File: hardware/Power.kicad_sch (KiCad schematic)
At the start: 16 parts, among them J200 Conn_Receptacle_2P, Q200 AO3401A, U200 RT9080-33GJ5, U201 TPS610997DRV, X200 12401598E4#2A

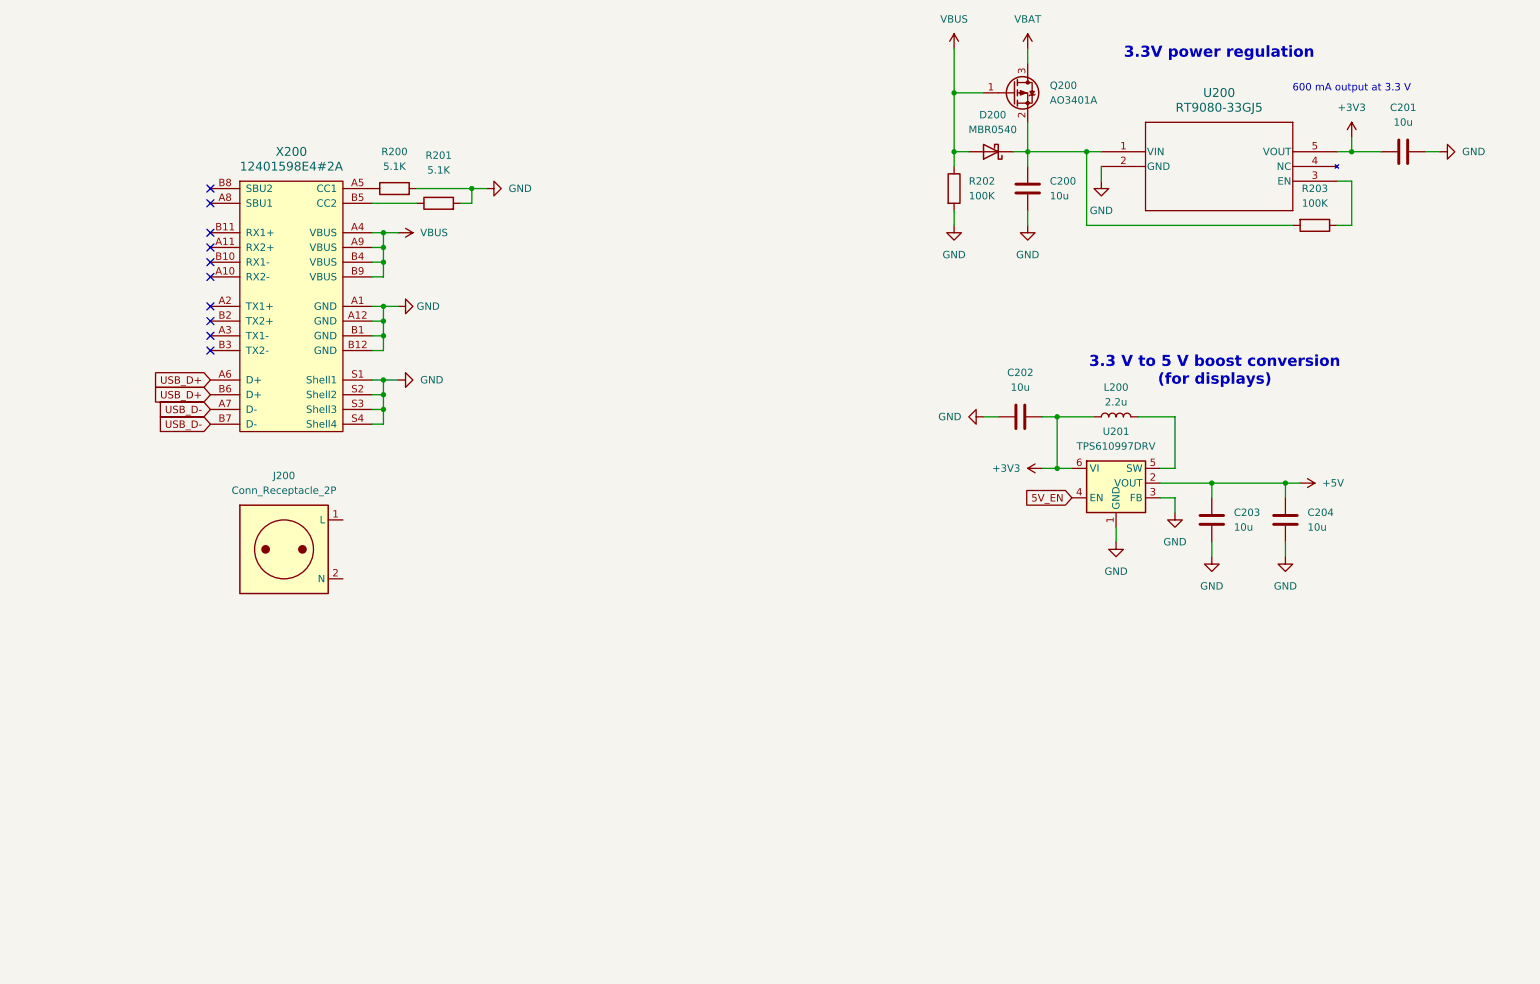
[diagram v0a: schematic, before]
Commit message: Modify 5V boost converter to use VBAT instead of 3V3 for input and add power switching circuit
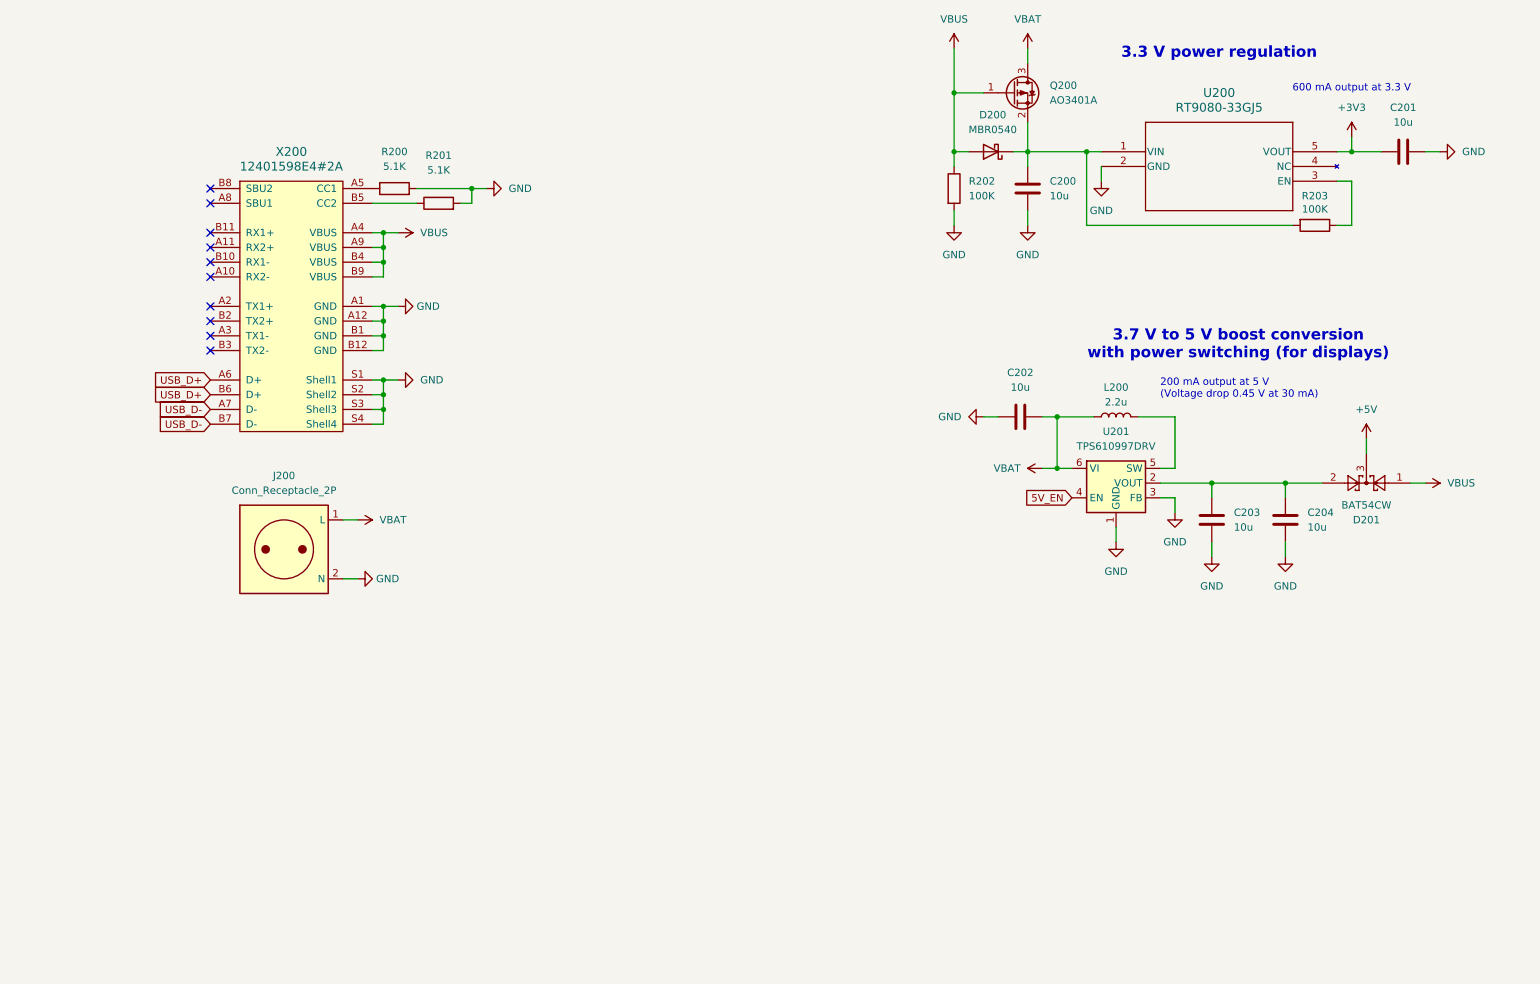
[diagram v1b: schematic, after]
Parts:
- added D201: BAT54CW, Package_TO_SOT_SMD:SOT-323_SC-70, symbol Diode:BAT54CW
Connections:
- net +3V3: no longer C202.2, L200.1, U201.6 (VI)
- net +5V: now also D201.3; no longer C203.1, C204.1, U201.2 (VOUT)
- net GND: now also J200.2 (N)
- net VBAT: now also C202.2, J200.1 (L), L200.1, U201.6 (VI)
- net VBUS: now also D201.1
- new net: C203.1, C204.1, D201.2, U201.2 (VOUT)
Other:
- note added: "200 mA output at 5 V (Voltage drop 0.45 V at 30 mA)"
- note added: "3.3 V power regulation"
- note added: "3.7 V to 5 V boost conversion with power switching (for displays)"
- note removed: "3.3 V to 5 V boost conversion (for displays)"
- note removed: "3.3V power regulation"

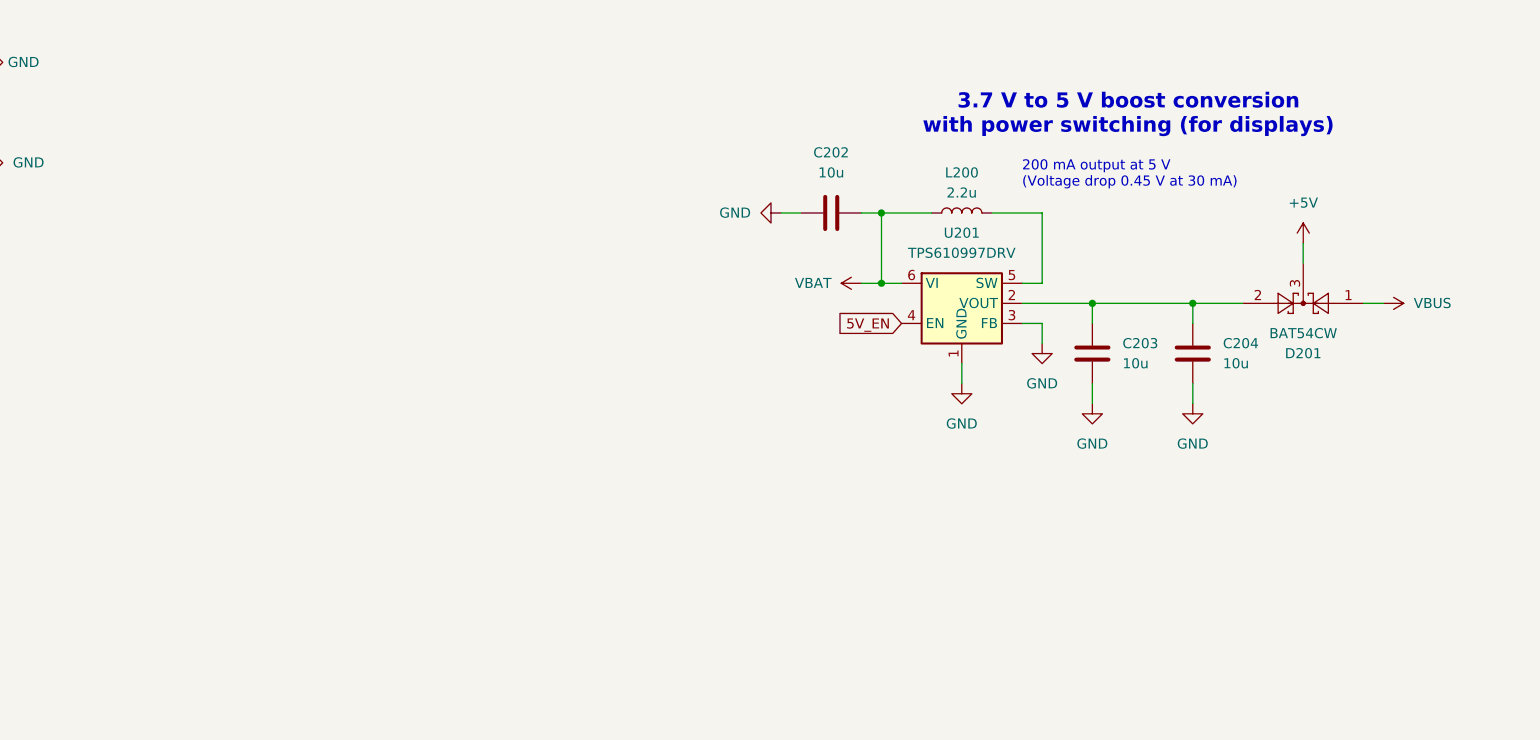
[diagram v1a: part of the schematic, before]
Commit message: Add voltage divider and replace boost converter
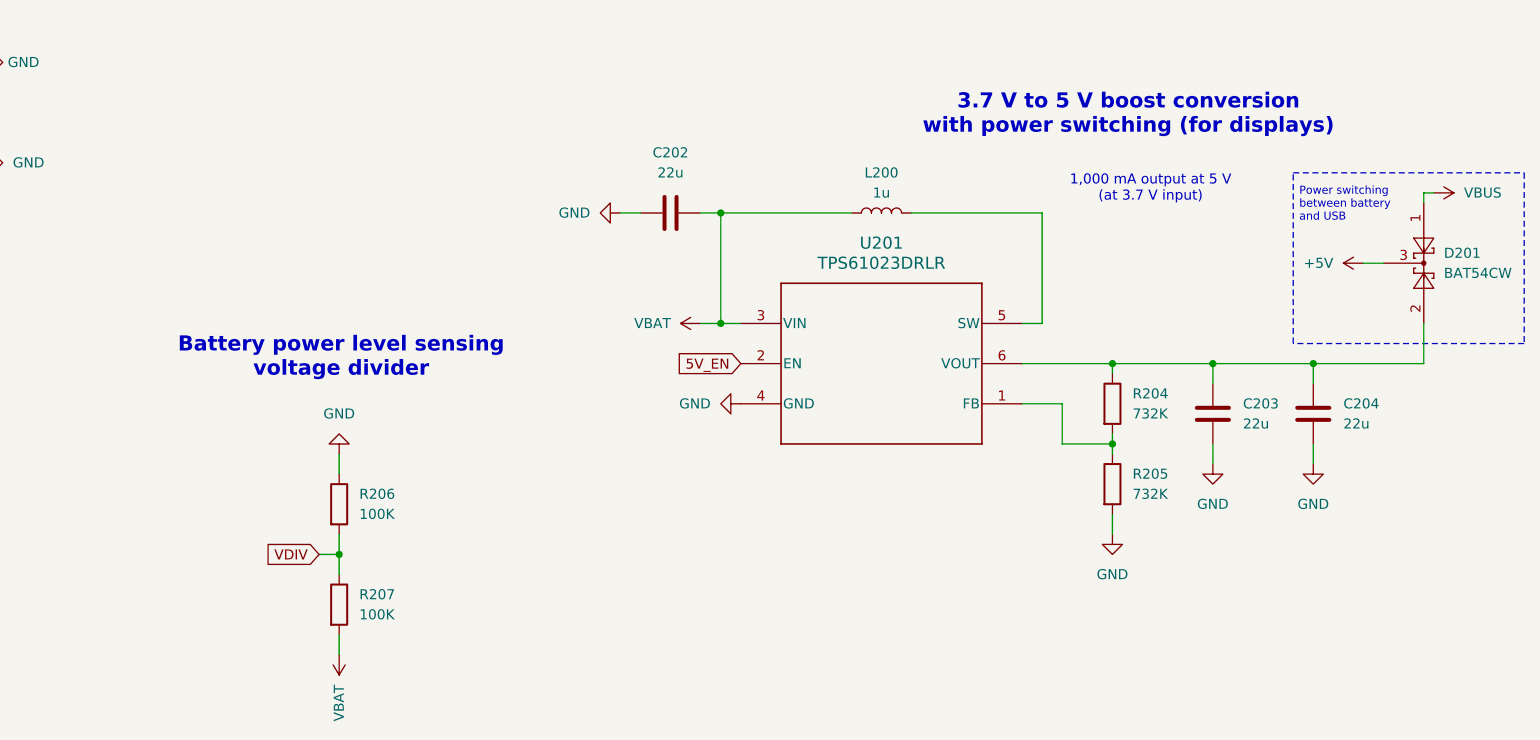
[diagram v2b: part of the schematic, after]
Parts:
- removed U201: TPS610997DRV, Package_SON:WSON-6-1EP_2x2mm_P0.65mm_EP1x1.6mm, symbol Regulator_Switching:TPS610997DRV
- added R204, R205: 732K, Resistor_SMD:R_0201_0603Metric_Pad0.64x0.40mm_HandSolder, symbol Device:R
- added R206, R207: 100K, Resistor_SMD:R_0201_0603Metric_Pad0.64x0.40mm_HandSolder, symbol Device:R
- added U201: TPS61023DRLR, TPS61023:DRL0006A, symbol TPS61023:TPS61023DRLR
- C202, C203, C204: value 10u -> 22u
- L200: value 2.2u -> 1u; footprint Inductor_SMD:L_0201_0603Metric_Pad0.64x0.40mm_HandSolder -> Inductor_SMD:L_1008_2520Metric_Pad1.43x2.20mm_HandSolder
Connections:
- net 5V_EN: now also U201.2 (EN)
- net GND: now also R205.2, R206.1, U201.4 (GND)
- net VBAT: now also R207.2, U201.3 (VIN)
- net at C203.1, C204.1, D201.2: now also R204.1, U201.6 (VOUT)
- net at L200.2: now also U201.5 (SW)
- new net: R204.2, R205.1, U201.1 (FB)
- new net VDIV: R206.2, R207.1
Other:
- note added: "1,000 mA output at 5 V (at 3.7 V input)"
- note added: "Battery power level sensing voltage divider"
- note added: "Power switching between battery and USB"
- note removed: "200 mA output at 5 V (Voltage drop 0.45 V at 30 mA)"
- moved on the sheet: C202, C203, C204, D201

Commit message: Add notes about voltage drop at +5V power switching circuit
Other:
- note added: "1,000 mA output at 5.2 V (at 3.7 V input)"
- note added: "5.2 V - 0.45 V = 4.75 V output"
- note added: "Voltage drop 0.45 V at 30 mA"
- note removed: "1,000 mA output at 5 V (at 3.7 V input)"
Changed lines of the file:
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@@
 		)
 	)
-	(text "1,000 mA output at 5 V\n(at 3.7 V input)"
+	(text "1,000 mA output at 5.2 V\n(at 3.7 V input)"
 		(exclude_from_sim no)
 		(at 230.886 90.932 0)
@@
 	(text "Power switching\nbetween battery\nand USB"
 		(exclude_from_sim no)
-		(at 249.682 92.964 0)
+		(at 249.682 90.424 0)
 		(effects
 			(font
 				(size 1.016 1.016)
 			)
-			(justify left)
+			(justify left top)
 		)
 	)
@@
 		)
 	)
+	(text "5.2 V - 0.45 V = 4.75 V output"
+		(exclude_from_sim no)
+		(at 247.904 100.584 0)
+		(effects
+			(font
+				(size 1.016 1.016)
+			)
+			(justify right)
+		)
+	)
+	(text "Voltage drop\n0.45 V at 30 mA"
+		(exclude_from_sim no)
+		(at 249.682 109.474 0)
+		(effects
+			(font
+				(size 1.016 1.016)
+			)
+			(justify left bottom)
+		)
+	)

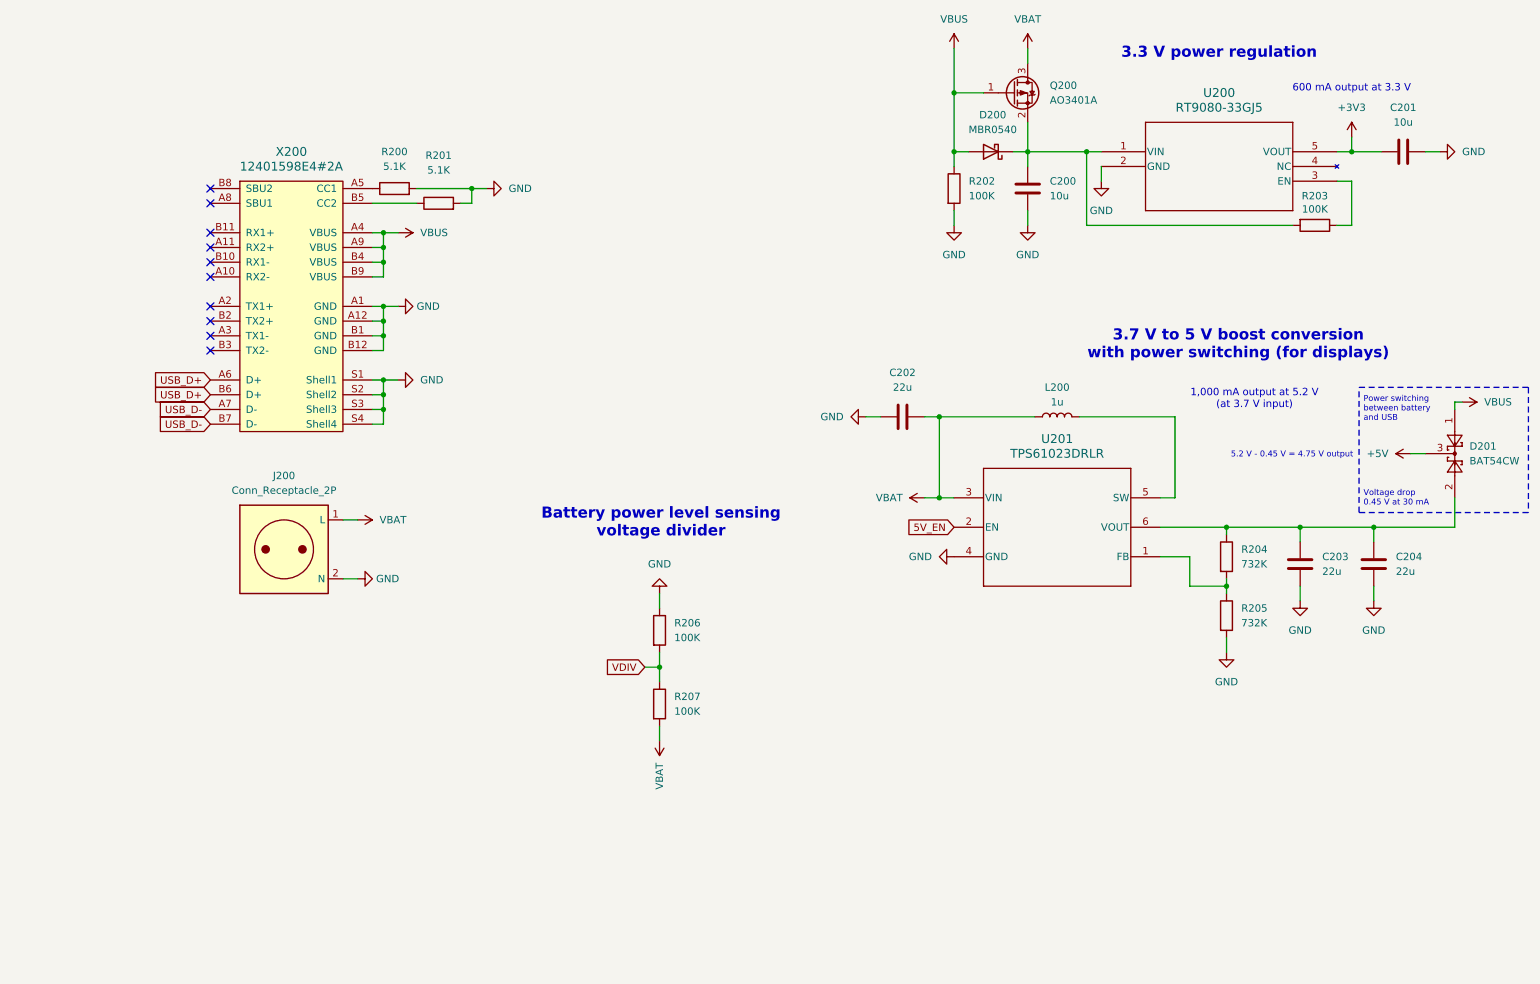
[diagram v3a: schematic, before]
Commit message: Add battery charging circuit
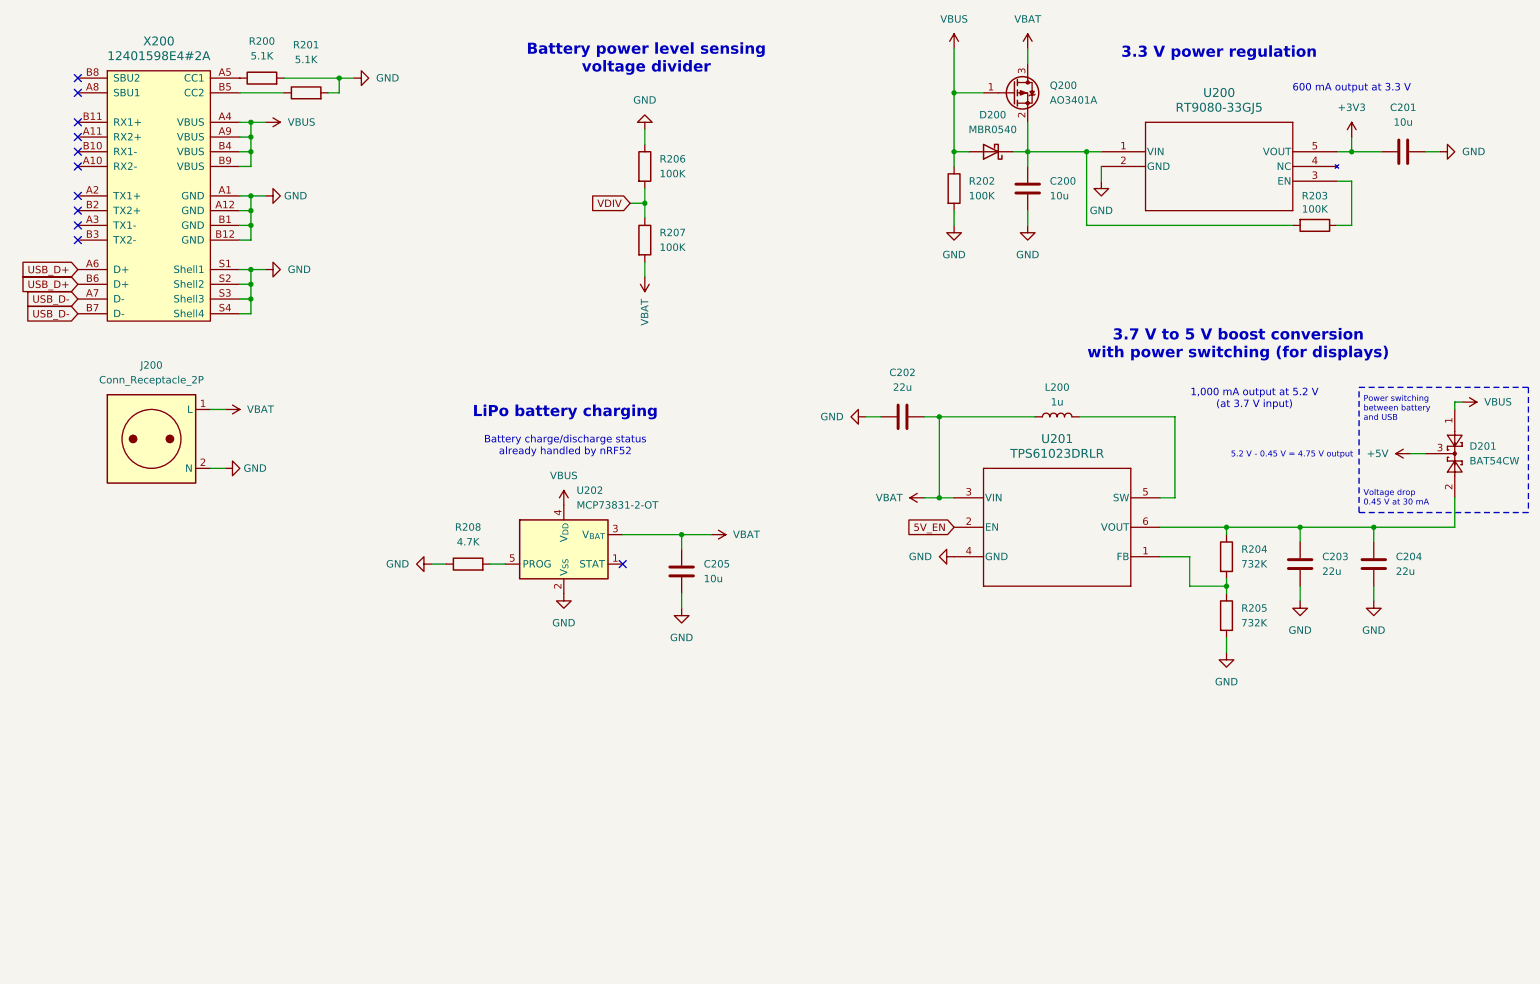
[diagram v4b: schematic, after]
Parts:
- added C205: 10u, Capacitor_SMD:C_0201_0603Metric_Pad0.64x0.40mm_HandSolder, symbol Device:C
- added R208: 4.7K, Resistor_SMD:R_0201_0603Metric_Pad0.64x0.40mm_HandSolder, symbol Device:R
- added U202: MCP73831-2-OT, Package_TO_SOT_SMD:SOT-23-5, symbol Battery_Management:MCP73831-2-OT
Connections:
- net GND: now also C205.2, R208.1, U202.2 (V_{SS})
- net VBAT: now also C205.1, U202.3 (V_{BAT})
- net VBUS: now also U202.4 (V_{DD})
- new net: R208.2, U202.5 (PROG)
- no-connect marks 10 -> 11
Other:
- note added: "Battery charge/discharge status already handled by nRF52"
- note added: "LiPo battery charging"
- moved on the sheet: J200, R200, R201, R206, R207, X200

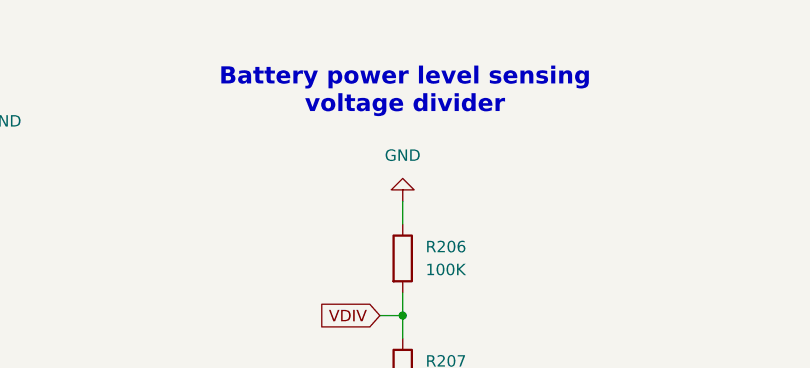
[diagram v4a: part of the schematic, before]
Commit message: Make a few minor adjustments and add headings to schematic
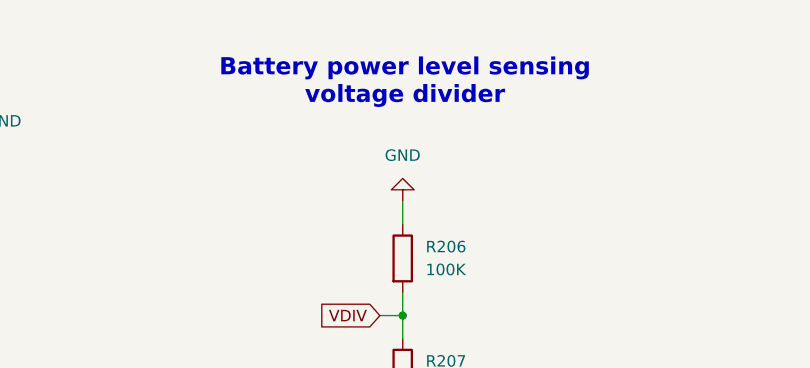
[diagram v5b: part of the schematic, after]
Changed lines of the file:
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@@
 	(text "Battery power level sensing\nvoltage divider"
 		(exclude_from_sim no)
-		(at 125.984 32.258 0)
+		(at 125.984 31.242 0)
 		(effects
 			(font
